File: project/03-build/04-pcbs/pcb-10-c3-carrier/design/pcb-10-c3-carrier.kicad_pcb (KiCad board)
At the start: 4 copper layers, 70 x 49.5 mm, 83 parts, among them J1 J10-1 +5 V (W11), J10 J10-10 rear TCRT (W36), J12 J10-12 readiness (W39, PCB-03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, J2 J10-2 base link (W25), J3 J10-3 encoder L (W30), J4 J10-4 encoder R (W31), J5 J10-5 left DRV8833 (W32), J6 J10-6 right DRV8833 (W33), J7 J10-7 IMU PCB-07 (W29), J8 J10-8 nose (W34), Q1 AO3400A, U1 ESP32-S3-DevKitC-1-N8, U2 THVD1451DR, U3 TPS3436CCCBGDDFRQ1, U4 74LVC1G08, U5 74LVC1G11

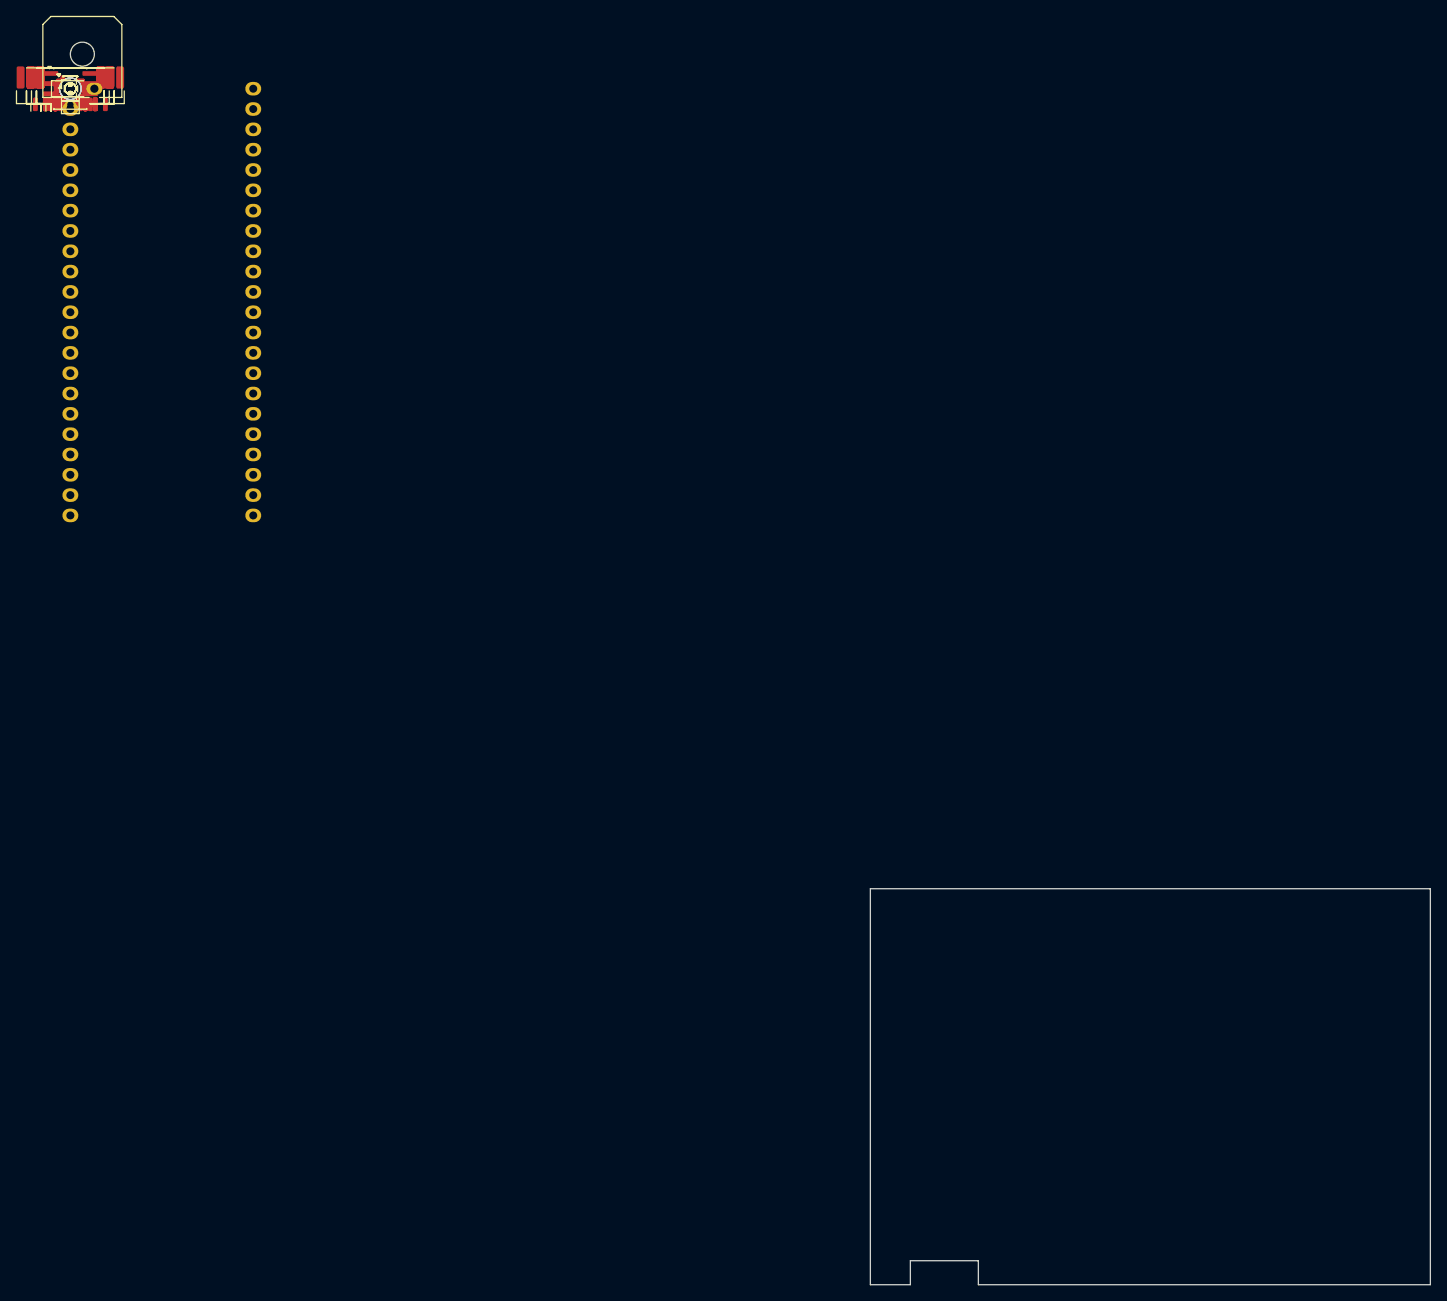
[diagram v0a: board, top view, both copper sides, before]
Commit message: build(pcbs): PCB-10 routed on four layers; DRC 0 errors, 0 unconnected, parity clean (lesson 4, part 2)
In1 solid GND, In2 +3V3 plane carrying WDO, C3_READY and SLP as tracks,
B for the top-row descents, UART and +5V_DK round the edges. Test points
cut to rails + WDI/WDO/C3_READY/SLP.

Co-Authored-By: Claude Opus 5.5 <noreply@anthropic.com>
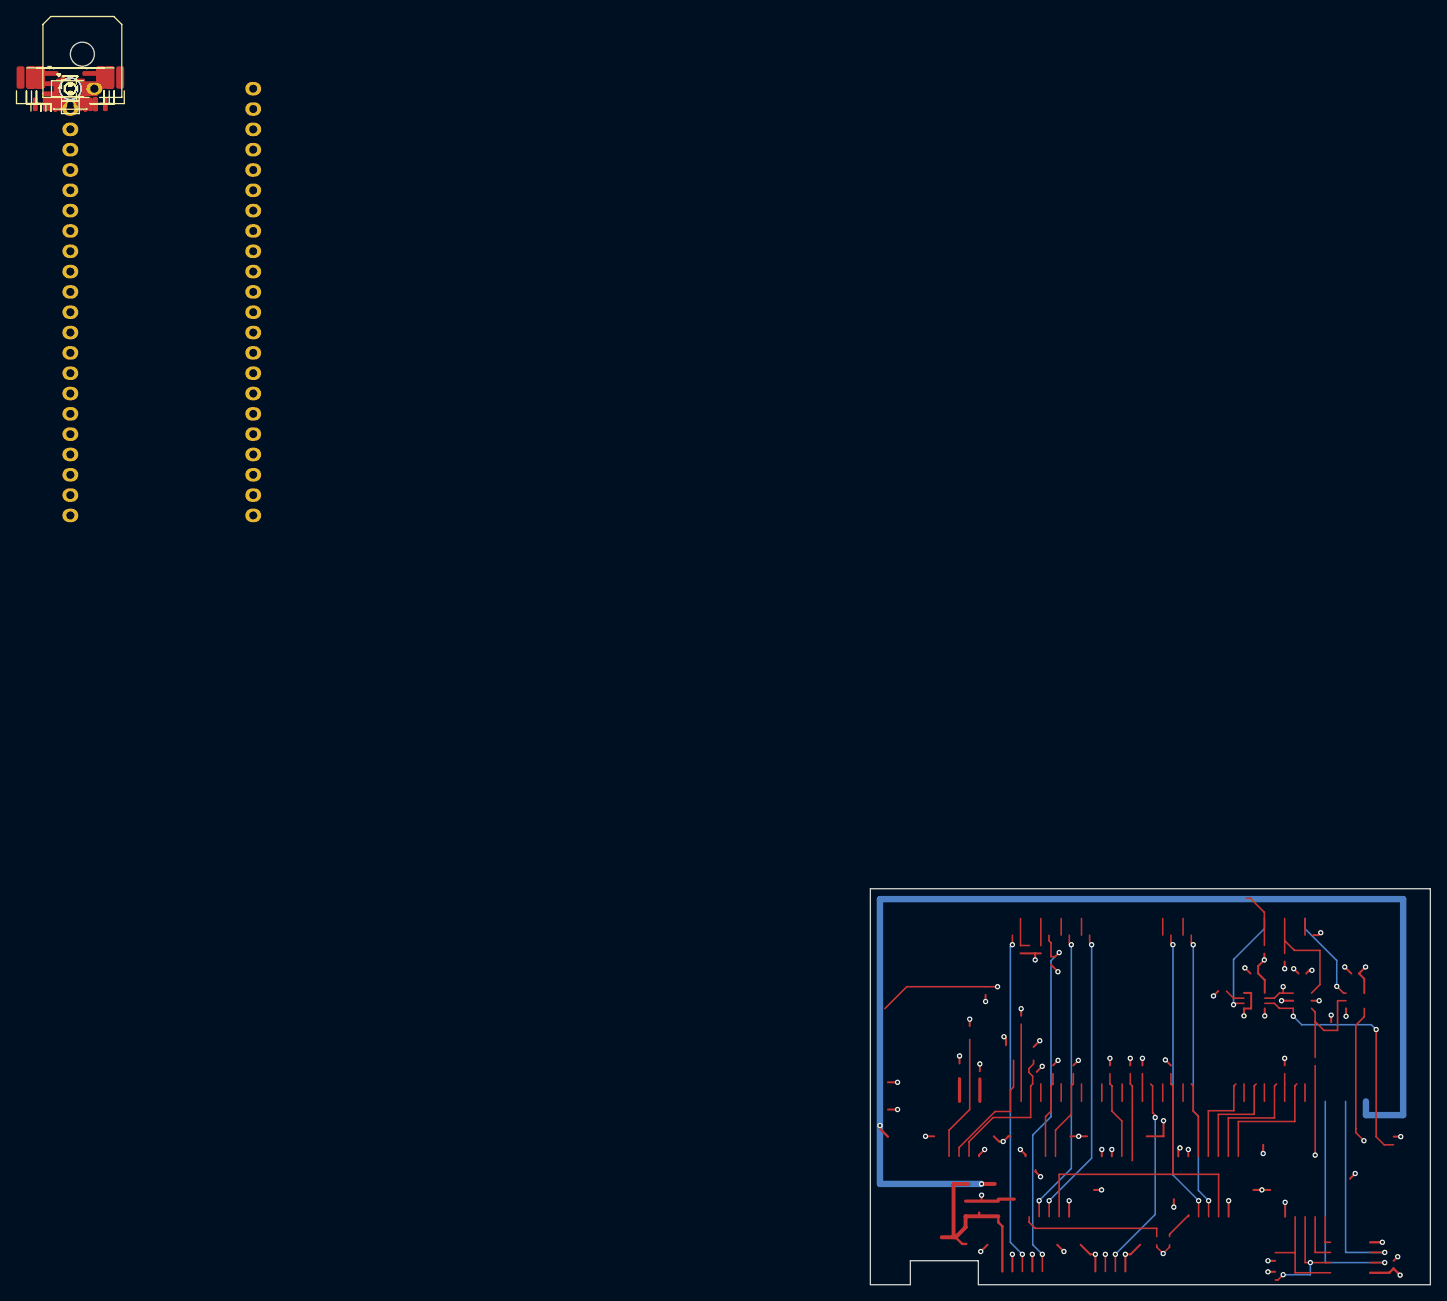
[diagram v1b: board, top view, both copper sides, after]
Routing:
- net /+5V_DK: track 0.00 -> 150.5 mm, vias 0 -> 2
- net /GND: track 0.00 -> 74.8 mm, vias 0 -> 44
- net /WDO: track 0.00 -> 69.9 mm, vias 0 -> 2
- net /SLP: track 0.00 -> 59.1 mm, vias 0 -> 2
- net /HALL_OUT: track 0.00 -> 45.8 mm, vias 0 -> 2
- net /C3_READY: track 0.00 -> 45.7 mm, vias 0 -> 2
- net /FLT: track 0.00 -> 43.2 mm
- net /GP2Y_VO: track 0.00 -> 42.8 mm, vias 0 -> 2
- net /+3V3: track 0.00 -> 38.5 mm, vias 0 -> 22
- net /IN2_R: track 0.00 -> 37.5 mm, vias 0 -> 2
- net /IN1_R: track 0.00 -> 37.0 mm, vias 0 -> 2
- net /IN1_L: track 0.00 -> 36.6 mm, vias 0 -> 2
- net /IN2_L: track 0.00 -> 36.1 mm, vias 0 -> 2
- net /WD_EN: track 0.00 -> 31.9 mm, vias 0 -> 2
- net /UART_RX: track 0.00 -> 29.4 mm, vias 0 -> 1
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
